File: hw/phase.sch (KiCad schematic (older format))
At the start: 9 parts

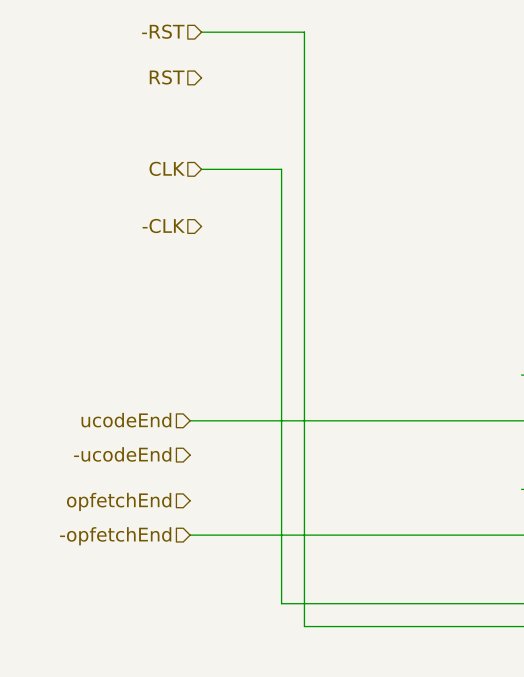
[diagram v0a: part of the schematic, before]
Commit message: clean up opfetch, finishing touches on phase logic
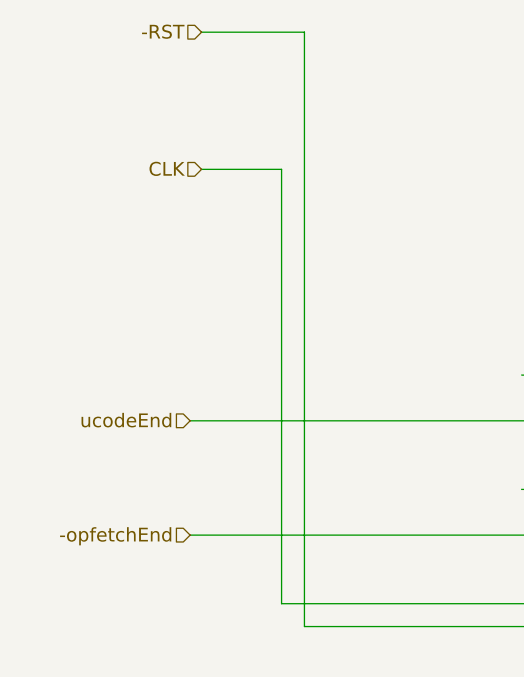
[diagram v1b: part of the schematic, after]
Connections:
- net labels removed: -CLK, -ucodeEnd, RST, opfetchEnd
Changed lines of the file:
@@
 Comment4 ""
 $EndDescr
-Text HLabel 1150 3600 0    60   Input ~ 0
-opfetchEnd
 Text HLabel 1150 3250 0    60   Input ~ 0
 ucodeEnd
@@
 Text HLabel 1200 1550 0    60   Input ~ 0
 -RST
-Text HLabel 1200 1750 0    60   Input ~ 0
-RST
 Text HLabel 1200 2150 0    60   Input ~ 0
 CLK
-Text HLabel 1200 2400 0    60   Input ~ 0
--CLK
 $Comp
 L 74LS175 U?
@@
 Text HLabel 1150 3750 0    60   Input ~ 0
 -opfetchEnd
-Text HLabel 1150 3400 0    60   Input ~ 0
--ucodeEnd
 Wire Wire Line
 	7700 3550 9000 3550
